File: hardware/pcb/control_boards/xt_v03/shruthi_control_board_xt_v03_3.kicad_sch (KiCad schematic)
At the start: 50 parts, among them IC2 74HC165N, IC3 74HC165N, IC8 74595N, IC9 74HC165N, SW1 Encoder

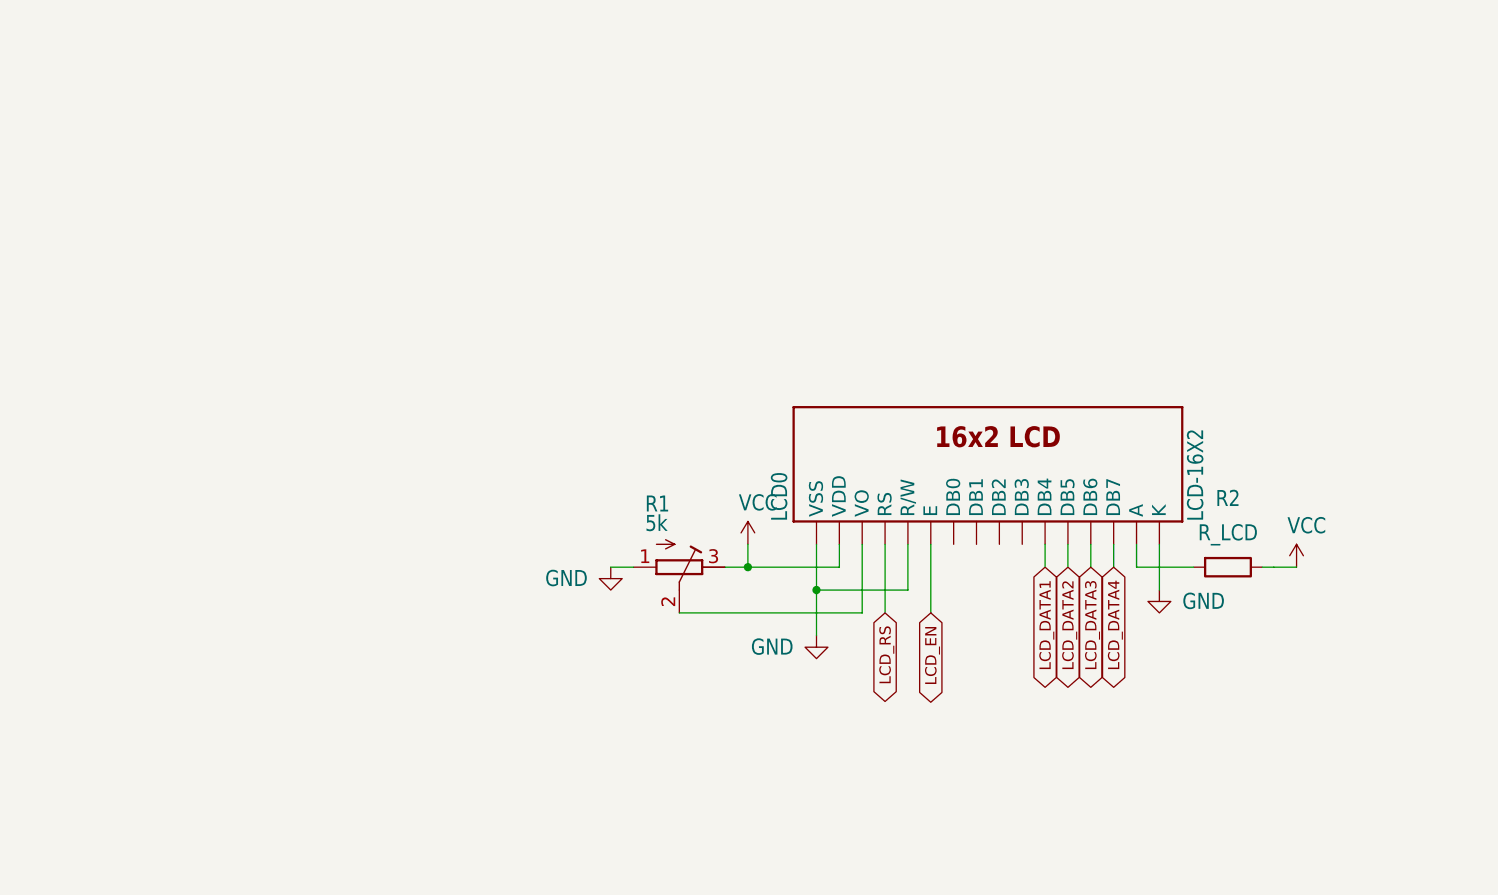
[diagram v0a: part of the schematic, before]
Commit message: update LCD parts to use kicad symbols
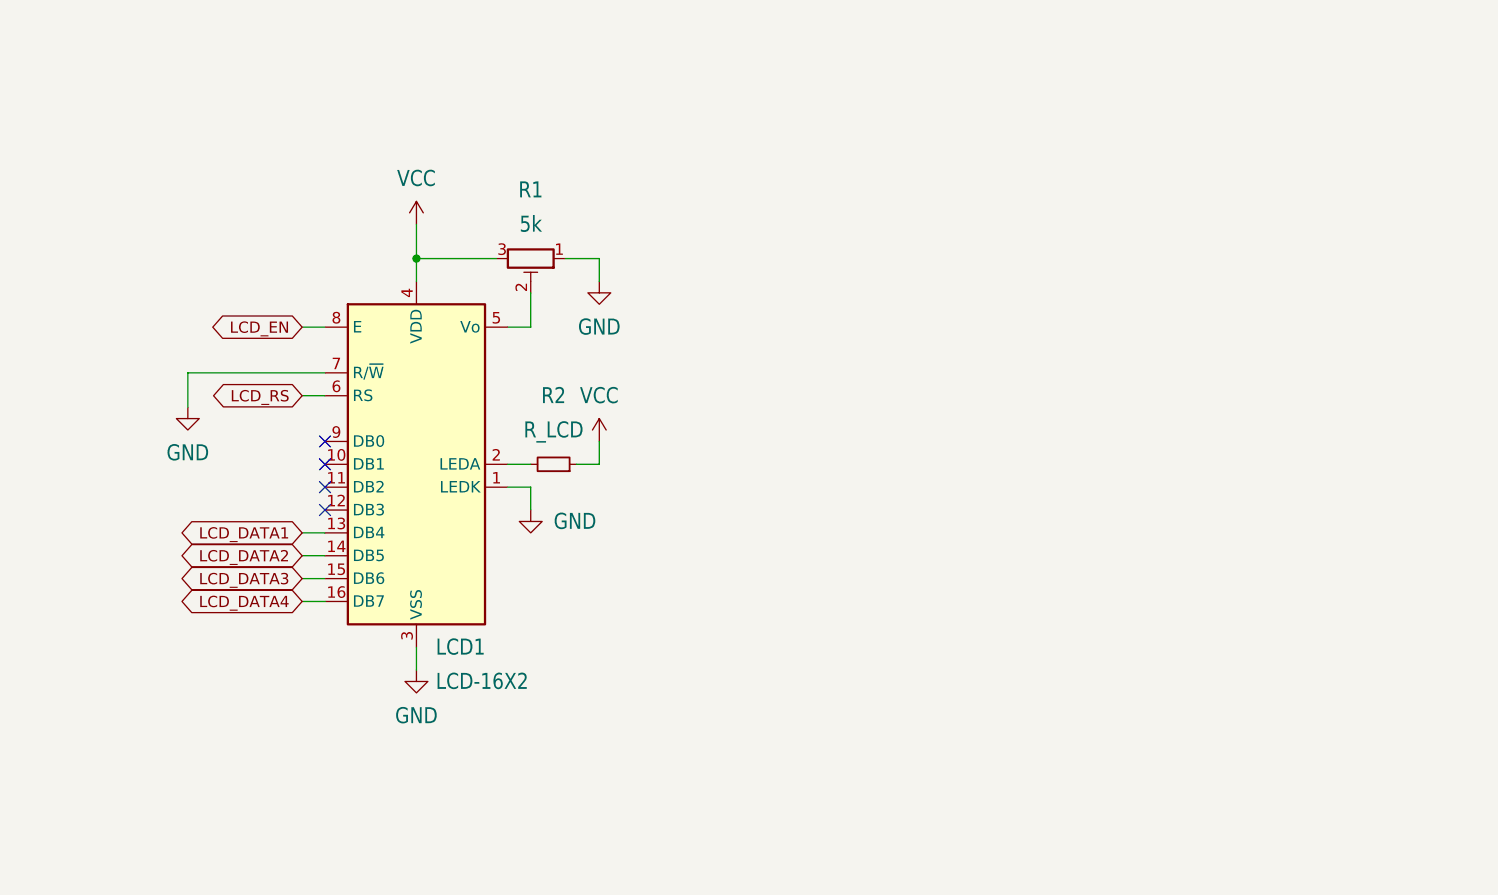
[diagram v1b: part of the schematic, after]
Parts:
- LCD1: renamed from LCD0; footprint shruthi_control_board_xt_v03:LCD-16X2 -> Display:HY1602E; symbol shruthi_control_board_xt_v03-eagle-import:LCD-16X2 -> Display_Character:HY1602E
- R1: symbol shruthi_control_board_xt_v03-eagle-import:R-TRIMM3339P -> Device:R_Potentiometer_Trim
- R2: symbol Device:R -> Device:R_Small
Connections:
- net GND: now also LCD1.3 (VSS), LCD1.7 (R/~{W}); no longer LCD1.16 (K), LCD1.5 (R/W)
- net LCD_DATA1: now also LCD1.13 (DB4); no longer LCD1.11 (DB4)
- net LCD_DATA2: now also LCD1.14 (DB5); no longer LCD1.12 (DB5)
- net LCD_DATA3: now also LCD1.15 (DB6); no longer LCD1.13 (DB6)
- net LCD_DATA4: now also LCD1.16 (DB7); no longer LCD1.14 (DB7)
- net LCD_EN: now also LCD1.8 (E); no longer LCD1.6 (E)
- net LCD_RS: now also LCD1.6 (RS); no longer LCD1.4 (RS)
- net VCC: now also LCD1.4 (VDD); no longer LCD1.2 (VDD)
- net at R2.2: now also LCD1.2 (LEDA); no longer LCD1.15 (A)
- net at R1.2: now also LCD1.5 (Vo); no longer LCD1.3 (VO)
- no-connect marks 8 -> 12
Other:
- moved on the sheet: R2

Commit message: use original LCD footprint for now
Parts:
- LCD1: footprint Display:HY1602E -> shruthi_control_board_xt_v03:LCD-16X2
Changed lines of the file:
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@@
 			)
 		)
-		(property "Footprint" "Display:HY1602E"
+		(property "Footprint" "shruthi_control_board_xt_v03:LCD-16X2"
 			(at 184.15 242.57 0)
 			(effects

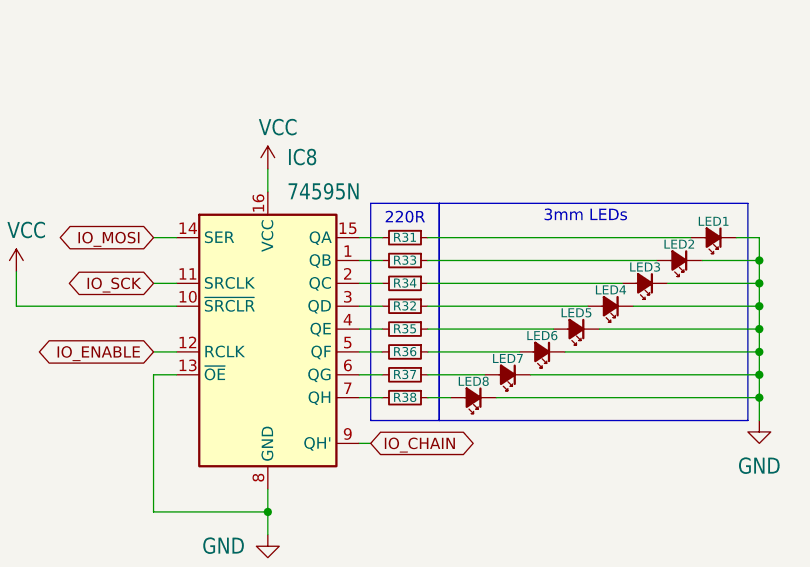
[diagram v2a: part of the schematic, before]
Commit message: update LED and LED resistor footprints
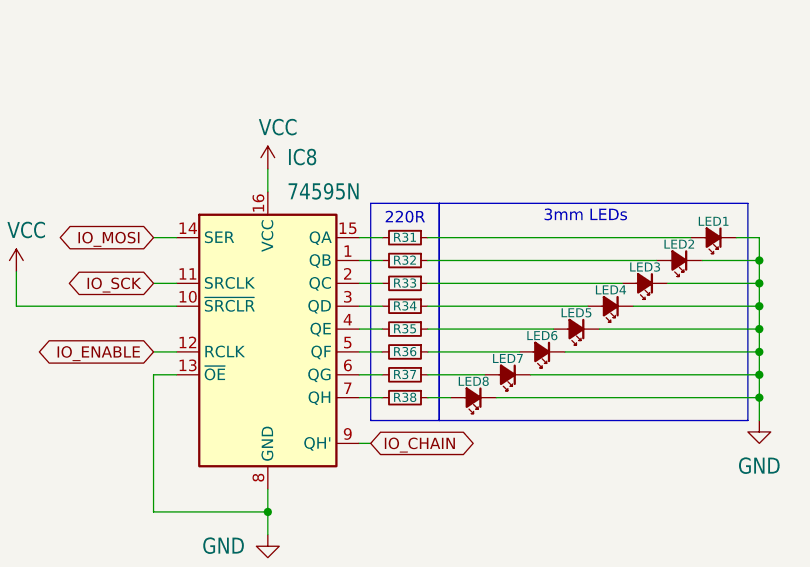
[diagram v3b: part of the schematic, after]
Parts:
- LED1, LED2, LED3, LED4, LED5, LED6, LED7, LED8: footprint shruthi_control_board_xt_v03:LED3MM -> LED_THT:LED_D3.0mm
- R31, R35, R36, R37, R38: footprint shruthi_control_board_xt_v03:0204_7 -> Resistor_THT:R_Axial_DIN0204_L3.6mm_D1.6mm_P7.62mm_Horizontal
- R32: renamed from R33; footprint shruthi_control_board_xt_v03:0204_7 -> Resistor_THT:R_Axial_DIN0204_L3.6mm_D1.6mm_P7.62mm_Horizontal
- R33: renamed from R34; footprint shruthi_control_board_xt_v03:0204_7 -> Resistor_THT:R_Axial_DIN0204_L3.6mm_D1.6mm_P7.62mm_Horizontal
- R34: renamed from R32; footprint shruthi_control_board_xt_v03:0204_7 -> Resistor_THT:R_Axial_DIN0204_L3.6mm_D1.6mm_P7.62mm_Horizontal
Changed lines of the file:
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@@
 			)
 		)
-		(property "Footprint" "shruthi_control_board_xt_v03:0204_7"
+		(property "Footprint" "Resistor_THT:R_Axial_DIN0204_L3.6mm_D1.6mm_P7.62mm_Horizontal"
 			(at 90.17 193.04 0)
 			(effects
@@
 			)
 		)
-		(property "Footprint" "shruthi_control_board_xt_v03:LED3MM"
+		(property "Footprint" "LED_THT:LED_D3.0mm"
 			(at 120.65 185.42 90)
 			(effects
@@
 		(on_board yes)
 		(dnp no)
-		(property "Reference" "R33"
+		(property "Reference" "R32"
 			(at 90.17 185.42 90)
 			(effects
@@
 			)
 		)
-		(property "Footprint" "shruthi_control_board_xt_v03:0204_7"
+		(property "Footprint" "Resistor_THT:R_Axial_DIN0204_L3.6mm_D1.6mm_P7.62mm_Horizontal"
 			(at 90.17 185.42 0)
 			(effects
@@
 			(project "shruthi_control_board_xt_v03"
 				(path "/2c840835-6e01-4901-947c-222cae369ab9/1e4cf160-db0f-4db8-aa2b-cf7d135880af"
-					(reference "R33")
+					(reference "R32")
 					(unit 1)
 				)
@@
 			)
 		)
-		(property "Footprint" "shruthi_control_board_xt_v03:LED3MM"
+		(property "Footprint" "LED_THT:LED_D3.0mm"
 			(at 101.6 198.12 90)
 			(effects
@@
 			)
 		)
-		(property "Footprint" "shruthi_control_board_xt_v03:LED3MM"
+		(property "Footprint" "LED_THT:LED_D3.0mm"
 			(at 105.41 195.58 90)
 			(effects
@@
 			)
 		)
-		(property "Footprint" "shruthi_control_board_xt_v03:0204_7"
+		(property "Footprint" "Resistor_THT:R_Axial_DIN0204_L3.6mm_D1.6mm_P7.62mm_Horizontal"
 			(at 90.17 198.12 0)
 			(effects
@@
 			)
 		)
-		(property "Footprint" "shruthi_control_board_xt_v03:0204_7"
+		(property "Footprint" "Resistor_THT:R_Axial_DIN0204_L3.6mm_D1.6mm_P7.62mm_Horizontal"
 			(at 90.17 182.88 0)
 			(effects
@@
 			)
 		)
-		(property "Footprint" "shruthi_control_board_xt_v03:LED3MM"
+		(property "Footprint" "LED_THT:LED_D3.0mm"
 			(at 116.84 187.96 90)
 			(effects
@@
 			)
 		)
-		(property "Footprint" "shruthi_control_board_xt_v03:0204_7"
+		(property "Footprint" "Resistor_THT:R_Axial_DIN0204_L3.6mm_D1.6mm_P7.62mm_Horizontal"
 			(at 90.17 195.58 0)
 			(effects
@@
 			)
 		)
-		(property "Footprint" "shruthi_control_board_xt_v03:LED3MM"
+		(property "Footprint" "LED_THT:LED_D3.0mm"
 			(at 113.03 190.5 90)
 			(effects
@@
 		(on_board yes)
 		(dnp no)
-		(property "Reference" "R34"
+		(property "Reference" "R33"
 			(at 90.17 187.96 90)
 			(effects
@@
 			)
 		)
-		(property "Footprint" "shruthi_control_board_xt_v03:0204_7"
+		(property "Footprint" "Resistor_THT:R_Axial_DIN0204_L3.6mm_D1.6mm_P7.62mm_Horizontal"
 			(at 90.17 187.96 0)
 			(effects
@@
 			(project "shruthi_control_board_xt_v03"
 				(path "/2c840835-6e01-4901-947c-222cae369ab9/1e4cf160-db0f-4db8-aa2b-cf7d135880af"
-					(reference "R34")
+					(reference "R33")
 					(unit 1)
 				)
@@
 			)
 		)
-		(property "Footprint" "shruthi_control_board_xt_v03:LED3MM"
+		(property "Footprint" "LED_THT:LED_D3.0mm"
 			(at 124.46 182.88 90)
 			(effects
@@
 			)
 		)
-		(property "Footprint" "shruthi_control_board_xt_v03:0204_7"
+		(property "Footprint" "Resistor_THT:R_Axial_DIN0204_L3.6mm_D1.6mm_P7.62mm_Horizontal"
 			(at 90.17 200.66 0)
 			(effects
@@
 			)
 		)
-		(property "Footprint" "shruthi_control_board_xt_v03:LED3MM"
+		(property "Footprint" "LED_THT:LED_D3.0mm"
 			(at 109.22 193.04 90)
 			(effects
@@
 			)
 		)
-		(property "Footprint" "shruthi_control_board_xt_v03:LED3MM"
+		(property "Footprint" "LED_THT:LED_D3.0mm"
 			(at 97.79 200.66 90)
 			(effects
@@
 		(on_board yes)
 		(dnp no)
-		(property "Reference" "R32"
+		(property "Reference" "R34"
 			(at 90.17 190.5 90)
 			(effects
@@
 			)
 		)
-		(property "Footprint" "shruthi_control_board_xt_v03:0204_7"
+		(property "Footprint" "Resistor_THT:R_Axial_DIN0204_L3.6mm_D1.6mm_P7.62mm_Horizontal"
 			(at 90.17 190.5 0)
 			(effects
@@
 			(project "shruthi_control_board_xt_v03"
 				(path "/2c840835-6e01-4901-947c-222cae369ab9/1e4cf160-db0f-4db8-aa2b-cf7d135880af"
-					(reference "R32")
+					(reference "R34")
 					(unit 1)
 				)

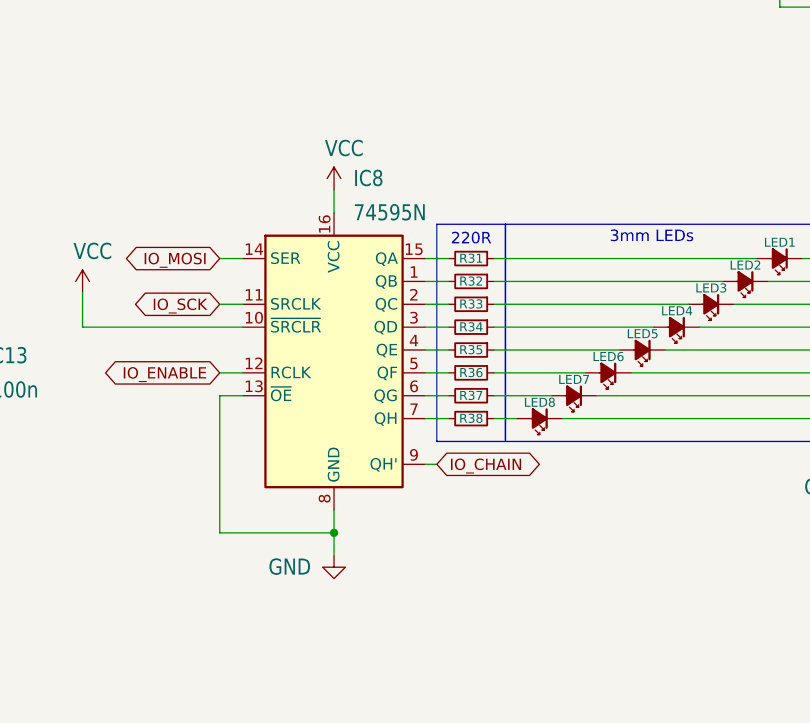
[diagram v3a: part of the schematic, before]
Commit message: update footprint for 74HC595
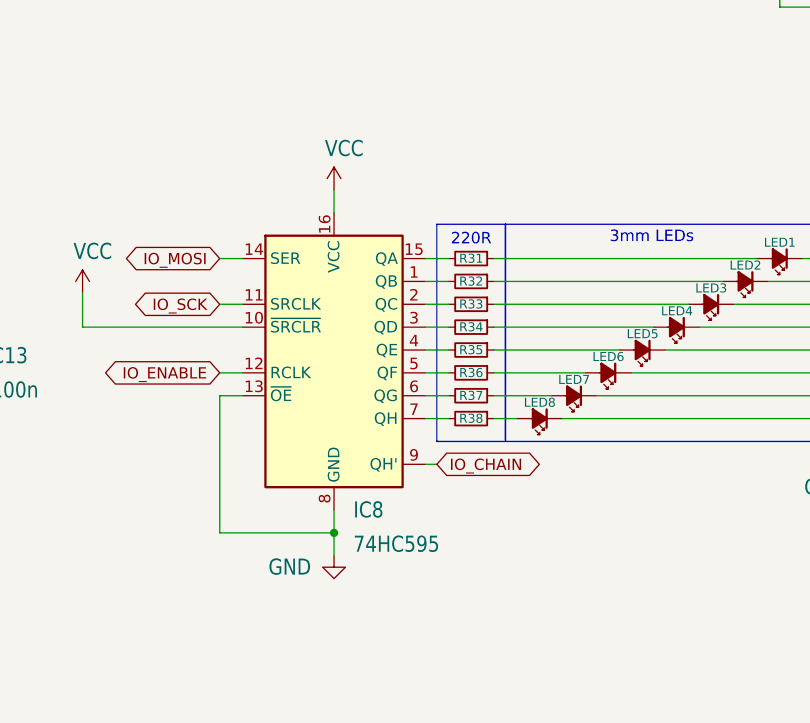
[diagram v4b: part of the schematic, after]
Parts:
- IC8: value 74595N -> 74HC595; footprint shruthi_control_board_xt_v03:DIL16 -> Package_DIP:DIP-16_W7.62mm_Socket_LongPads
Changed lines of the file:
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@@
 		(fields_autoplaced yes)
 		(property "Reference" "IC8"
-			(at 77.0733 173.99 0)
+			(at 77.0733 210.82 0)
 			(effects
 				(font
@@
 			)
 		)
-		(property "Value" "74595N"
-			(at 77.0733 177.8 0)
+		(property "Value" "74HC595"
+			(at 77.0733 214.63 0)
 			(effects
 				(font
@@
 			)
 		)
-		(property "Footprint" "shruthi_control_board_xt_v03:DIL16"
+		(property "Footprint" "Package_DIP:DIP-16_W7.62mm_Socket_LongPads"
 			(at 74.93 193.04 0)
 			(effects

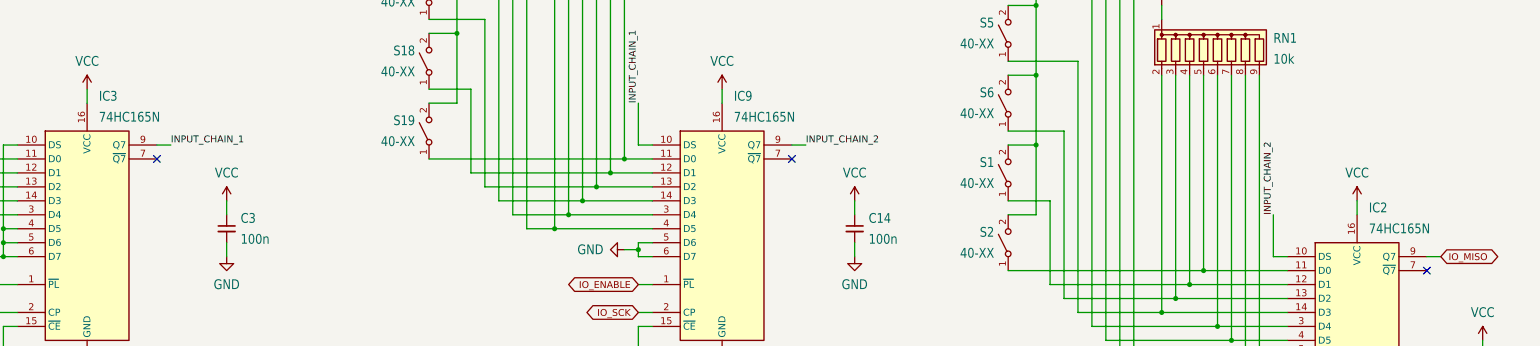
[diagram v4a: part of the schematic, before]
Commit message: update silkscreen for 74HC165s
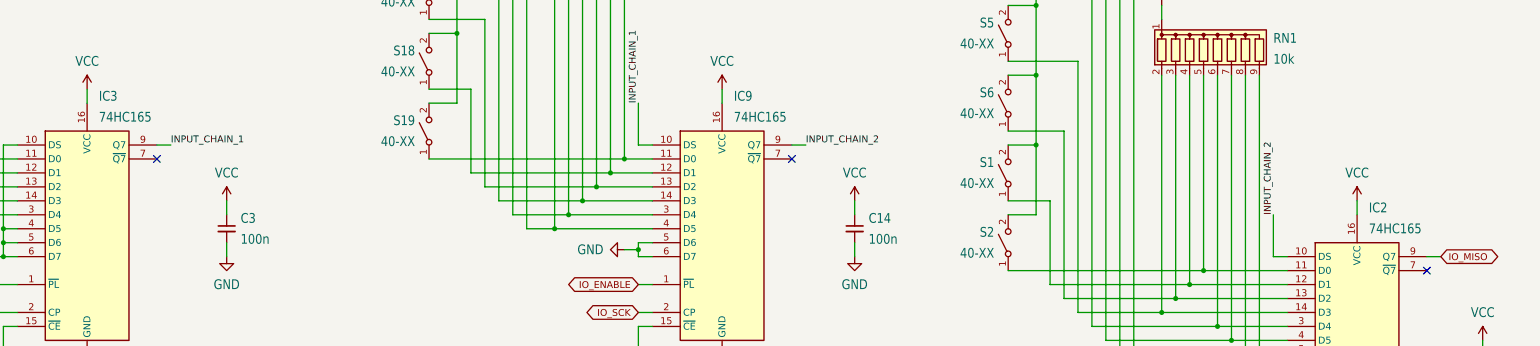
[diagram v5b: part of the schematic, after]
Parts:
- IC2, IC3, IC9: value 74HC165N -> 74HC165
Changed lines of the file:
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@@
 			)
 		)
-		(property "Value" "74HC165N"
+		(property "Value" "74HC165"
 			(at 141.8433 106.68 0)
 			(effects
@@
 			)
 		)
-		(property "Value" "74HC165N"
+		(property "Value" "74HC165"
 			(at 257.4133 106.68 0)
 			(effects
@@
 			)
 		)
-		(property "Value" "74HC165N"
+		(property "Value" "74HC165"
 			(at 372.9833 127 0)
 			(effects
